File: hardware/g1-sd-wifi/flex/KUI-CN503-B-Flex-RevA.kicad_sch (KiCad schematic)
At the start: 2 parts, among them J1 CN503 row B solder contacts, J2 20-pin bottom-contact FPC tail

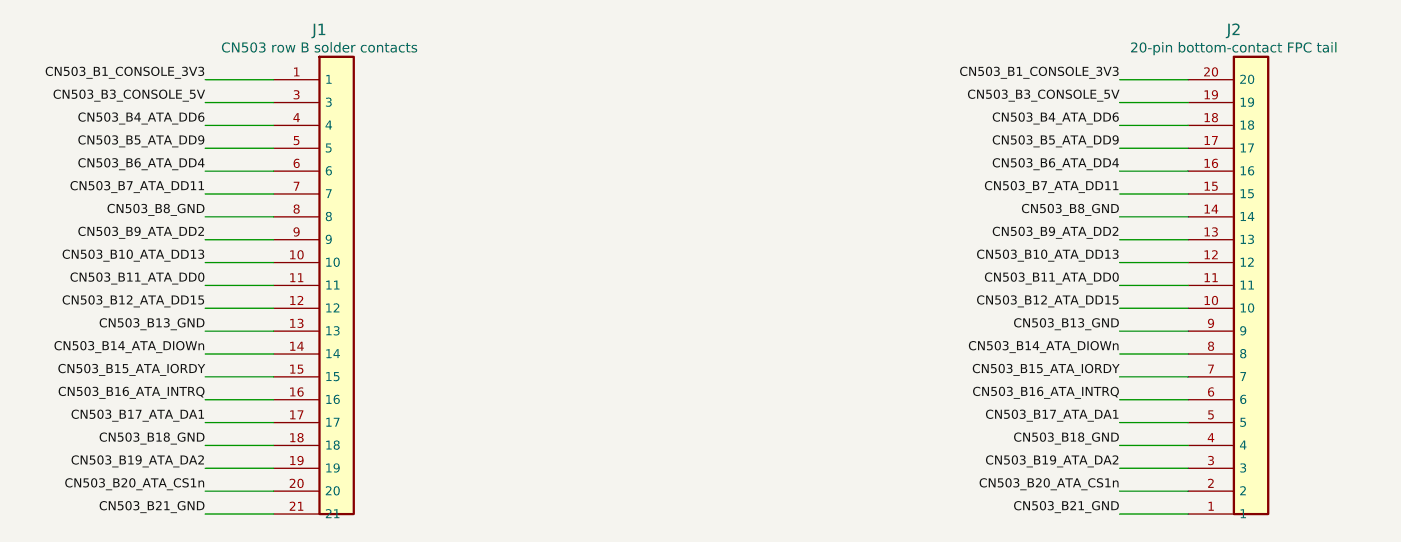
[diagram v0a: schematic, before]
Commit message: G1 safety: fuse the host 3.3-V entry; no console 5 V on the flex or carrier
Host 3.3 V reached about 30 carrier parts straight from two flex contacts,
and the two console-5-V contacts were joined by an unused carrier trace;
a short on either would load a console supply through 0.5 A connector
contacts with no fuse anywhere. Now:

- F21 (0467.500NR, 0.5 A fast, same 467 family as F20) sits between the one
  remaining 3.3-V entry, J51 B1, and CONSOLE_3V3. If it opens the buffers
  lose VCCB and isolate, and U25 reports the host rail absent.
- CN503 A1 (second 3.3 V) and A3/B3 (5 V) get no flex copper at all: no
  landing pad, no trace, only an unconnected mating finger, so a chafed
  flex cannot short a console supply. Their carrier socket pins are bare.
  flex-interface.json lists them; the flex and carrier generators and both
  checks read that list. Flex ERC/DRC/parity 0; carrier ERC 0, integration
  check pass (362 parts).
- The DSN export keeps the 5-V and storage supply nets on the 1 oz outer
  layers: on 0.5 oz inner copper a 0.25 mm track at the fuse current would
  overheat (IPC-2221).
- F21 is placed by the floorplan next to J51; board DRC 0, parity 0
  (unrouted).

Co-Authored-By: Claude Opus 5.5 <noreply@anthropic.com>
Claude-Session: https://claude.ai/code/session_01Gp9EYc2r9fMpZ7V8WtfonZ
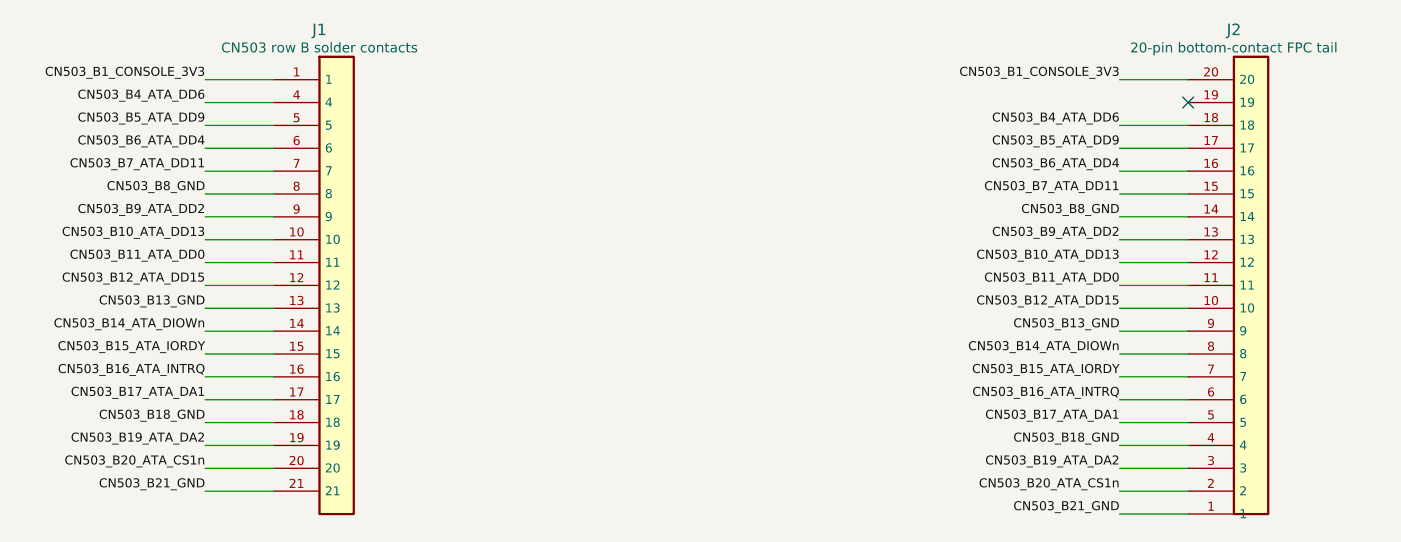
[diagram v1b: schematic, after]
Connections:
- net CN503_B3_CONSOLE_5V: no longer names the net of J2.19
- net CN503_B3_CONSOLE_5V: no longer J1.3
- no-connect marks 0 -> 1
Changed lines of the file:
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@@
 (wire (pts (xy 71.12 109.22) (xy 63.5 109.22)) (stroke (width 0) (type default)))
 (wire (pts (xy 71.12 111.76) (xy 63.5 111.76)) (stroke (width 0) (type default)))
-(wire (pts (xy 71.12 114.3) (xy 63.5 114.3)) (stroke (width 0) (type default)))
 (wire (pts (xy 172.72 66.04) (xy 165.10000000000002 66.04)) (stroke (width 0) (type default)))
-(wire (pts (xy 172.72 68.58) (xy 165.10000000000002 68.58)) (stroke (width 0) (type default)))
 (wire (pts (xy 172.72 71.12) (xy 165.10000000000002 71.12)) (stroke (width 0) (type default)))
 (wire (pts (xy 172.72 73.66) (xy 165.10000000000002 73.66)) (stroke (width 0) (type default)))
@@
 (wire (pts (xy 172.72 114.3) (xy 165.10000000000002 114.3)) (stroke (width 0) (type default)))
 (label "CN503_B1_CONSOLE_3V3" (at 63.5 66.04 0) (effects (font (size 1 1)) (justify right bottom)))
-(label "CN503_B3_CONSOLE_5V" (at 63.5 68.58 0) (effects (font (size 1 1)) (justify right bottom)))
-(label "CN503_B4_ATA_DD6" (at 63.5 71.12 0) (effects (font (size 1 1)) (justify right bottom)))
-(label "CN503_B5_ATA_DD9" (at 63.5 73.66 0) (effects (font (size 1 1)) (justify right bottom)))
-(label "CN503_B6_ATA_DD4" (at 63.5 76.2 0) (effects (font (size 1 1)) (justify right bottom)))
-(label "CN503_B7_ATA_DD11" (at 63.5 78.74 0) (effects (font (size 1 1)) (justify right bottom)))
-(label "CN503_B8_GND" (at 63.5 81.28 0) (effects (font (size 1 1)) (justify right bottom)))
-(label "CN503_B9_ATA_DD2" (at 63.5 83.82 0) (effects (font (size 1 1)) (justify right bottom)))
-(label "CN503_B10_ATA_DD13" (at 63.5 86.36 0) (effects (font (size 1 1)) (justify right bottom)))
-(label "CN503_B11_ATA_DD0" (at 63.5 88.9 0) (effects (font (size 1 1)) (justify right bottom)))
-(label "CN503_B12_ATA_DD15" (at 63.5 91.44 0) (effects (font (size 1 1)) (justify right bottom)))
-(label "CN503_B13_GND" (at 63.5 93.98 0) (effects (font (size 1 1)) (justify right bottom)))
-(label "CN503_B14_ATA_DIOWn" (at 63.5 96.52 0) (effects (font (size 1 1)) (justify right bottom)))
-(label "CN503_B15_ATA_IORDY" (at 63.5 99.06 0) (effects (font (size 1 1)) (justify right bottom)))
-(label "CN503_B16_ATA_INTRQ" (at 63.5 101.6 0) (effects (font (size 1 1)) (justify right bottom)))
-(label "CN503_B17_ATA_DA1" (at 63.5 104.14 0) (effects (font (size 1 1)) (justify right bottom)))
-(label "CN503_B18_GND" (at 63.5 106.68 0) (effects (font (size 1 1)) (justify right bottom)))
-(label "CN503_B19_ATA_DA2" (at 63.5 109.22 0) (effects (font (size 1 1)) (justify right bottom)))
-(label "CN503_B20_ATA_CS1n" (at 63.5 111.76 0) (effects (font (size 1 1)) (justify right bottom)))
-(label "CN503_B21_GND" (at 63.5 114.3 0) (effects (font (size 1 1)) (justify right bottom)))
+(label "CN503_B4_ATA_DD6" (at 63.5 68.58 0) (effects (font (size 1 1)) (justify right bottom)))
+(label "CN503_B5_ATA_DD9" (at 63.5 71.12 0) (effects (font (size 1 1)) (justify right bottom)))
+(label "CN503_B6_ATA_DD4" (at 63.5 73.66 0) (effects (font (size 1 1)) (justify right bottom)))
+(label "CN503_B7_ATA_DD11" (at 63.5 76.2 0) (effects (font (size 1 1)) (justify right bottom)))
+(label "CN503_B8_GND" (at 63.5 78.74 0) (effects (font (size 1 1)) (justify right bottom)))
+(label "CN503_B9_ATA_DD2" (at 63.5 81.28 0) (effects (font (size 1 1)) (justify right bottom)))
+(label "CN503_B10_ATA_DD13" (at 63.5 83.82 0) (effects (font (size 1 1)) (justify right bottom)))
+(label "CN503_B11_ATA_DD0" (at 63.5 86.36 0) (effects (font (size 1 1)) (justify right bottom)))
+(label "CN503_B12_ATA_DD15" (at 63.5 88.9 0) (effects (font (size 1 1)) (justify right bottom)))
+(label "CN503_B13_GND" (at 63.5 91.44 0) (effects (font (size 1 1)) (justify right bottom)))
+(label "CN503_B14_ATA_DIOWn" (at 63.5 93.98 0) (effects (font (size 1 1)) (justify right bottom)))
+(label "CN503_B15_ATA_IORDY" (at 63.5 96.52 0) (effects (font (size 1 1)) (justify right bottom)))
+(label "CN503_B16_ATA_INTRQ" (at 63.5 99.06 0) (effects (font (size 1 1)) (justify right bottom)))
+(label "CN503_B17_ATA_DA1" (at 63.5 101.6 0) (effects (font (size 1 1)) (justify right bottom)))
+(label "CN503_B18_GND" (at 63.5 104.14 0) (effects (font (size 1 1)) (justify right bottom)))
+(label "CN503_B19_ATA_DA2" (at 63.5 106.68 0) (effects (font (size 1 1)) (justify right bottom)))
+(label "CN503_B20_ATA_CS1n" (at 63.5 109.22 0) (effects (font (size 1 1)) (justify right bottom)))
+(label "CN503_B21_GND" (at 63.5 111.76 0) (effects (font (size 1 1)) (justify right bottom)))
 (label "CN503_B1_CONSOLE_3V3" (at 165.10000000000002 66.04 0) (effects (font (size 1 1)) (justify right bottom)))
-(label "CN503_B3_CONSOLE_5V" (at 165.10000000000002 68.58 0) (effects (font (size 1 1)) (justify right bottom)))
 (label "CN503_B4_ATA_DD6" (at 165.10000000000002 71.12 0) (effects (font (size 1 1)) (justify right bottom)))
 (label "CN503_B5_ATA_DD9" (at 165.10000000000002 73.66 0) (effects (font (size 1 1)) (justify right bottom)))
@@
 (label "CN503_B20_ATA_CS1n" (at 165.10000000000002 111.76 0) (effects (font (size 1 1)) (justify right bottom)))
 (label "CN503_B21_GND" (at 165.10000000000002 114.3 0) (effects (font (size 1 1)) (justify right bottom)))
+(no_connect (at 172.72 68.58))
 (symbol (lib_id "KUI_Flex:CN503_B_Landing") (at 76.2 63.5 0) (unit 1) (in_bom no) (on_board yes) (dnp no)
 (property "Reference" "J1" (at 76.2 60.5 0) (effects (font (size 1.27 1.27))))
@@
 (property "Datasheet" "" (at 0 0 0) (effects (font (size 1.27 1.27)) hide))
 (pin "1")
-(pin "3")
 (pin "4")
 (pin "5")
